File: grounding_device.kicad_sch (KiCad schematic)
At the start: 118 parts, among them IC1 NE555P, IC2 NE555P, IC3 NE555P, IC4 NE555P, Q1 2N2222, Q10 2N2222, Q11 2N2222, Q12 2N2222, Q2 2N2222, Q3 2N2222, Q4 2N2222, Q5 2N2222, Q6 2N2222, Q7 2N2222, Q8 2N2222, Q9 2N2222

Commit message: Upgrade
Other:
- note added: "04.09.2023"
- moved on the sheet: R41
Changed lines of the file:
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@@
   (junction (at 110.49 130.81) (diameter 0) (color 0 0 0 0)
   )
-  (junction (at 261.62 127) (diameter 0) (color 0 0 0 0)
-  )
   (junction (at 99.06 69.85) (diameter 0) (color 0 0 0 0)
   )
@@
   (junction (at 106.68 107.95) (diameter 0) (color 0 0 0 0)
   )
-  (junction (at 264.16 95.25) (diameter 0) (color 0 0 0 0)
-  )
   (junction (at 133.35 15.24) (diameter 0) (color 0 0 0 0)
   )
@@
   (junction (at 217.17 48.26) (diameter 0) (color 0 0 0 0)
   )
+  (junction (at 264.16 48.26) (diameter 0) (color 0 0 0 0)
+  )
   (junction (at 189.23 120.65) (diameter 0) (color 0 0 0 0)
   )
@@
   (junction (at 177.8 95.25) (diameter 0) (color 0 0 0 0)
   )
+  (junction (at 250.19 83.82) (diameter 0) (color 0 0 0 0)
+  )
   (junction (at 115.57 44.45) (diameter 0) (color 0 0 0 0)
   )
@@
     (stroke (width 0) (type default))
   )
+  (wire (pts (xy 279.4 92.71) (xy 250.19 92.71))
+    (stroke (width 0) (type default))
+  )
   (wire (pts (xy 158.75 66.04) (xy 162.56 66.04))
     (stroke (width 0) (type default))
@@
     (stroke (width 0) (type default))
   )
+  (wire (pts (xy 250.19 83.82) (xy 255.27 83.82))
+    (stroke (width 0) (type default))
+  )
   (wire (pts (xy 96.52 83.82) (xy 130.81 83.82))
     (stroke (width 0) (type default))
@@
     (stroke (width 0) (type default))
   )
-  (wire (pts (xy 281.94 113.03) (xy 281.94 127))
-    (stroke (width 0) (type default))
-  )
   (wire (pts (xy 127 166.37) (xy 127 182.88))
     (stroke (width 0) (type default))
@@
     (stroke (width 0) (type default))
   )
-  (wire (pts (xy 281.94 127) (xy 261.62 127))
-    (stroke (width 0) (type default))
-  )
   (wire (pts (xy 139.7 48.26) (xy 154.94 48.26))
     (stroke (width 0) (type default))
@@
     (stroke (width 0) (type default))
   )
+  (wire (pts (xy 250.19 92.71) (xy 250.19 83.82))
+    (stroke (width 0) (type default))
+  )
   (wire (pts (xy 250.19 99.06) (xy 264.16 99.06))
     (stroke (width 0) (type default))
@@
     (stroke (width 0) (type default))
   )
+  (wire (pts (xy 264.16 48.26) (xy 279.4 48.26))
+    (stroke (width 0) (type default))
+  )
   (wire (pts (xy 160.02 104.14) (xy 160.02 93.98))
     (stroke (width 0) (type default))
@@
     (stroke (width 0) (type default))
   )
-  (wire (pts (xy 220.98 83.82) (xy 255.27 83.82))
+  (wire (pts (xy 220.98 83.82) (xy 250.19 83.82))
     (stroke (width 0) (type default))
   )
@@
     (stroke (width 0) (type default))
   )
-  (wire (pts (xy 281.94 95.25) (xy 281.94 102.87))
+  (wire (pts (xy 279.4 48.26) (xy 279.4 82.55))
     (stroke (width 0) (type default))
   )
@@
     (stroke (width 0) (type default))
   )
-  (wire (pts (xy 264.16 95.25) (xy 281.94 95.25))
-    (stroke (width 0) (type default))
-  )
   (wire (pts (xy 256.54 66.04) (xy 256.54 50.8))
     (stroke (width 0) (type default))
@@
     (effects (font (size 1.27 1.27)) (justify left bottom))
   )
+  (text "04.09.2023" (at 270.51 179.07 0)
+    (effects (font (size 1.27 1.27)) (justify left bottom))
+  )
   (text "Klimenko Maxim Sergievich" (at 223.52 185.42 0)
     (effects (font (size 1.27 1.27)) (justify left bottom))
@@
     )
   )
-  (symbol (lib_id "PCM_Elektuur:R") (at 281.94 107.95 0) (mirror y) (unit 1)
+  (symbol (lib_id "PCM_Elektuur:R") (at 279.4 87.63 0) (mirror y) (unit 1)
     (in_bom yes) (on_board yes) (dnp no) (fields_autoplaced)
-    (property "Reference" "R41" (at 279.4 106.68 0)
+    (property "Reference" "R41" (at 276.86 86.36 0)
       (effects (font (size 1.27 1.27)) (justify left))
     )
-    (property "Value" "10-9.5 MOM" (at 279.4 109.22 0)
+    (property "Value" "10-9.5 MOM" (at 276.86 88.9 0)
       (effects (font (size 1.27 1.27)) (justify left))
     )
-    (property "Footprint" "" (at 281.94 107.95 0)
+    (property "Footprint" "" (at 279.4 87.63 0)
       (effects (font (size 1.27 1.27)) hide)
     )
-    (property "Datasheet" "" (at 281.94 107.95 0)
+    (property "Datasheet" "" (at 279.4 87.63 0)
       (effects (font (size 1.27 1.27)) hide)
     )
-    (property "Indicator" "+" (at 285.115 104.775 0)
+    (property "Indicator" "+" (at 282.575 84.455 0)
       (effects (font (size 1.27 1.27)) hide)
     )
-    (property "Rating" "W" (at 279.4 111.125 0)
+    (property "Rating" "W" (at 276.86 90.805 0)
       (effects (font (size 1.27 1.27)) (justify left) hide)
     )

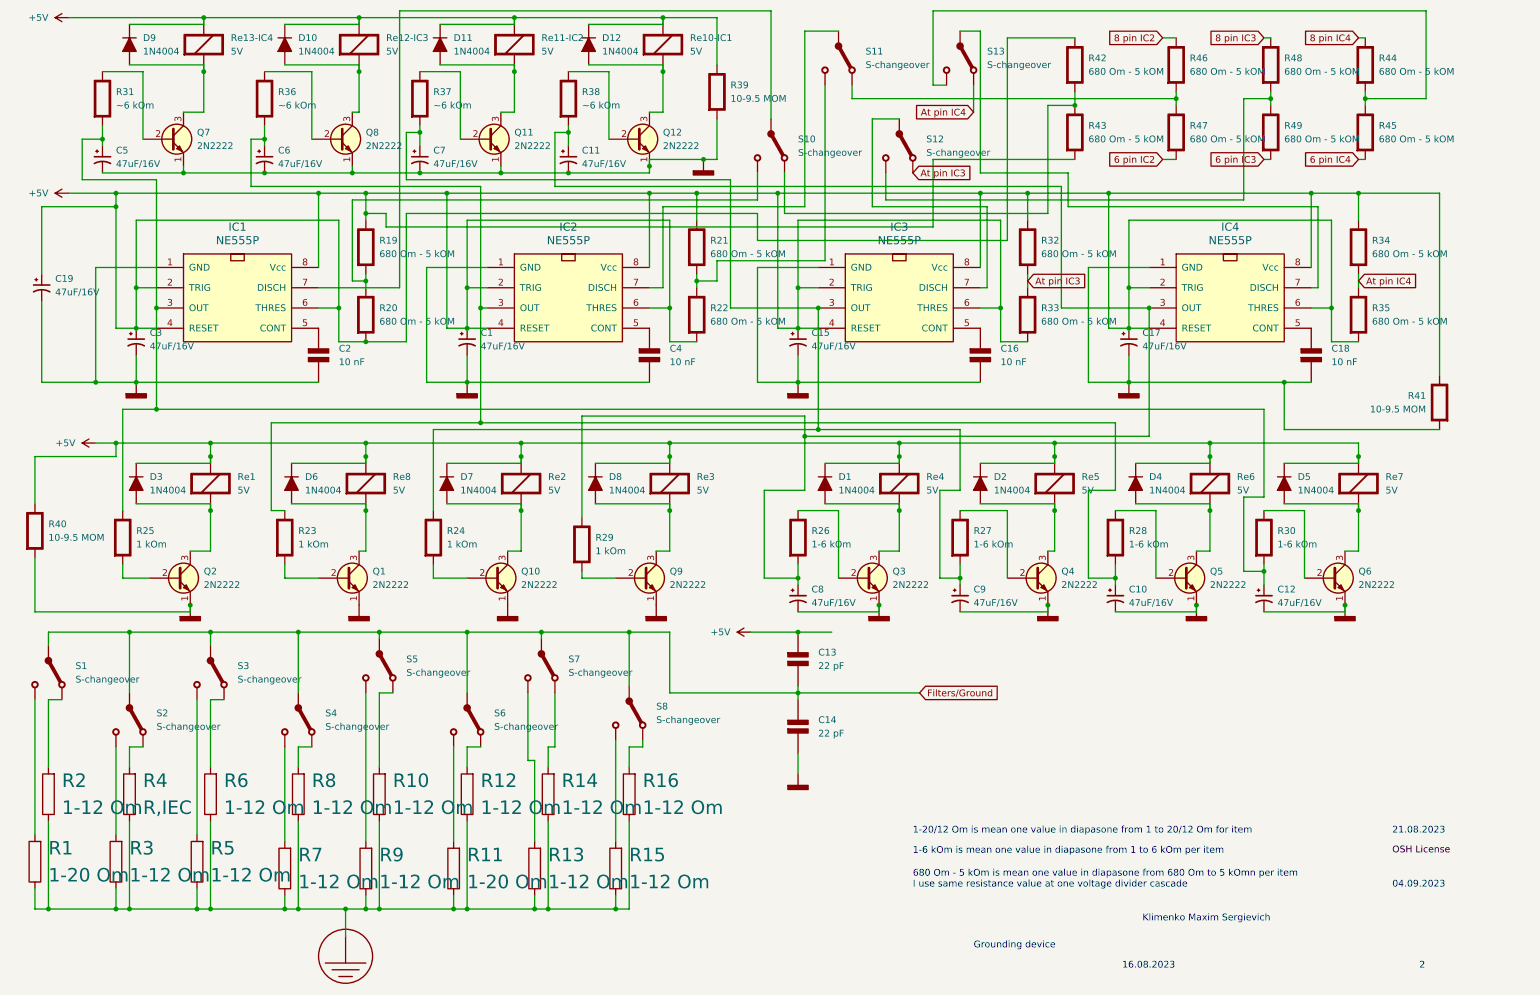
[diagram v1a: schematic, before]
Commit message: Fixed errors in capacitors values
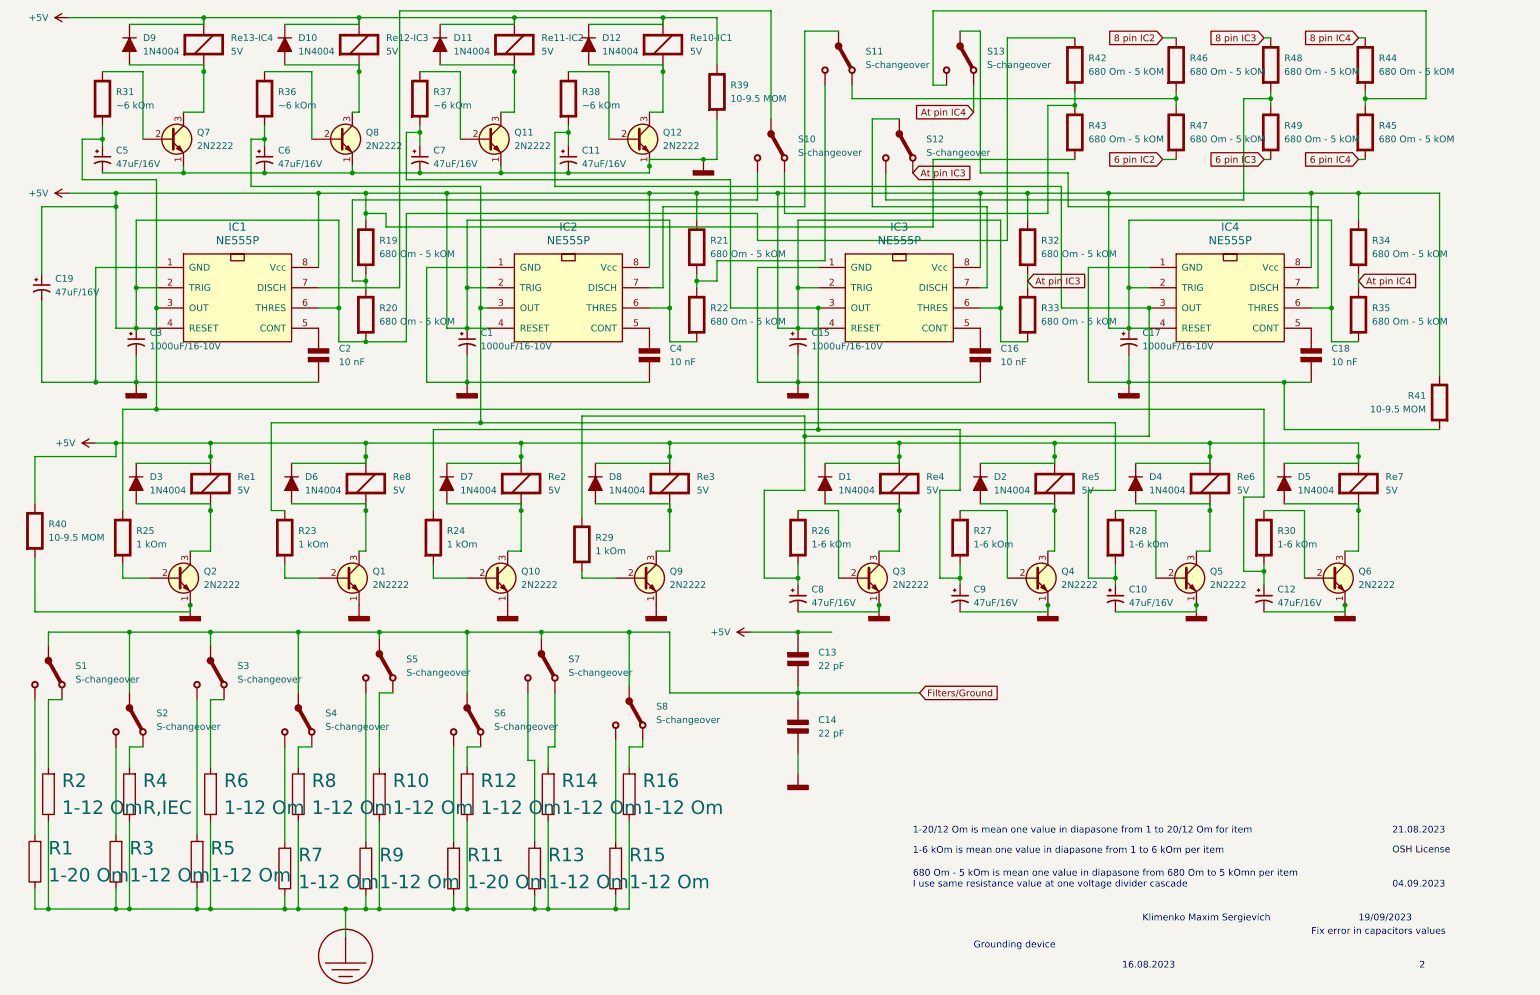
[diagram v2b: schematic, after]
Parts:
- C1, C15, C17, C3: Display 47uF/16V -> 1000uF/16-10V
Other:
- note added: "19/09/2023"
- note added: "Fix error in capacitors values"
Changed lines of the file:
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@@
     (effects (font (size 1.27 1.27)) (justify left bottom))
   )
+  (text "19/09/2023\n" (at 264.16 185.42 0)
+    (effects (font (size 1.27 1.27)) (justify left bottom))
+  )
   (text "Grounding device" (at 191.77 190.5 0)
     (effects (font (size 1.27 1.27)) (justify left bottom))
@@
     (effects (font (size 1.27 1.27)) (justify left bottom))
   )
+  (text "Fix error in capacitors values" (at 255.27 187.96 0)
+    (effects (font (size 1.27 1.27)) (justify left bottom))
+  )
   (label "OSH License" (at 270.51 172.72 0) (fields_autoplaced)
     (effects (font (size 1.27 1.27)) (justify left bottom))
@@
       (effects (font (size 1.27 1.27)) (justify left) hide)
     )
-    (property "Display" "47uF/16V" (at 99.06 77.0382 0)
+    (property "Display" "1000uF/16-10V" (at 99.06 77.0382 0)
       (effects (font (size 1.27 1.27)) (justify left))
     )
@@
       (effects (font (size 1.27 1.27)) (justify left) hide)
     )
-    (property "Display" "47uF/16V" (at 161.29 77.0382 0)
+    (property "Display" "1000uF/16-10V" (at 161.29 77.0382 0)
       (effects (font (size 1.27 1.27)) (justify left))
     )
@@
       (effects (font (size 1.27 1.27)) (justify left) hide)
     )
-    (property "Display" "47uF/16V" (at 36.83 77.0382 0)
+    (property "Display" "1000uF/16-10V" (at 36.83 77.0382 0)
       (effects (font (size 1.27 1.27)) (justify left))
     )
@@
       (effects (font (size 1.27 1.27)) (justify left) hide)
     )
-    (property "Display" "47uF/16V" (at 223.52 77.0382 0)
+    (property "Display" "1000uF/16-10V" (at 223.52 77.0382 0)
       (effects (font (size 1.27 1.27)) (justify left))
     )

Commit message: Fix
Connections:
- net +5V: no longer C1.1, C15.1, C17.1, C3.1, IC1.2 (TRIG), IC1.6 (THRES), IC2.2 (TRIG), IC2.6 (THRES), IC3.2 (TRIG), IC3.6 (THRES), IC4.2 (TRIG), IC4.6 (THRES), R20.2 (-), R22.2 (-), R33.2 (-), R35.2 (-), R42.1 (+)
- new net: C15.1, IC3.2 (TRIG), IC3.6 (THRES), R33.2 (-)
- new net: C1.1, IC2.2 (TRIG), IC2.6 (THRES), R22.2 (-)
- new net: C17.1, IC4.2 (TRIG), IC4.6 (THRES), R35.2 (-)
- new net: C3.1, IC1.2 (TRIG), IC1.6 (THRES), R20.2 (-), R42.1 (+)
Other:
- note added: "680 Om - 5 kOm is mean one value in diapasone from 680 Om to 5 kOmn per item I use same resistance value at one voltage divider cascade ( atennuator )"
- note removed: "680 Om - 5 kOm is mean one value in diapasone from 680 Om to 5 kOmn per item I use same resistance value at one voltage divider cascade"
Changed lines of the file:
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@@
   (junction (at 99.06 69.85) (diameter 0) (color 0 0 0 0)
   )
-  (junction (at 34.29 73.66) (diameter 0) (color 0 0 0 0)
-  )
   (junction (at 106.68 107.95) (diameter 0) (color 0 0 0 0)
   )
@@
   (junction (at 76.2 15.24) (diameter 0) (color 0 0 0 0)
   )
-  (junction (at 158.75 73.66) (diameter 0) (color 0 0 0 0)
-  )
   (junction (at 264.16 97.79) (diameter 0) (color 0 0 0 0)
   )
@@
   (junction (at 45.72 182.88) (diameter 0) (color 0 0 0 0)
   )
-  (junction (at 220.98 73.66) (diameter 0) (color 0 0 0 0)
-  )
   (junction (at 43.18 44.45) (diameter 0) (color 0 0 0 0)
   )
@@
   (junction (at 92.71 48.26) (diameter 0) (color 0 0 0 0)
   )
-  (junction (at 96.52 73.66) (diameter 0) (color 0 0 0 0)
-  )
   (junction (at 46.99 15.24) (diameter 0) (color 0 0 0 0)
   )
@@
     (stroke (width 0) (type default))
   )
-  (wire (pts (xy 34.29 73.66) (xy 30.48 73.66))
+  (wire (pts (xy 30.48 73.66) (xy 38.1 73.66))
     (stroke (width 0) (type default))
   )
@@
     (stroke (width 0) (type default))
   )
-  (wire (pts (xy 220.98 73.66) (xy 217.17 73.66))
+  (wire (pts (xy 217.17 73.66) (xy 224.79 73.66))
     (stroke (width 0) (type default))
   )
@@
     (stroke (width 0) (type default))
   )
-  (wire (pts (xy 158.75 73.66) (xy 154.94 73.66))
-    (stroke (width 0) (type default))
-  )
-  (wire (pts (xy 162.56 73.66) (xy 158.75 73.66))
+  (wire (pts (xy 154.94 73.66) (xy 162.56 73.66))
     (stroke (width 0) (type default))
   )
@@
     (stroke (width 0) (type default))
   )
-  (wire (pts (xy 38.1 73.66) (xy 34.29 73.66))
-    (stroke (width 0) (type default))
-  )
   (wire (pts (xy 152.4 104.14) (xy 160.02 104.14))
     (stroke (width 0) (type default))
@@
     (stroke (width 0) (type default))
   )
-  (wire (pts (xy 224.79 73.66) (xy 220.98 73.66))
-    (stroke (width 0) (type default))
-  )
   (wire (pts (xy 30.48 50.8) (xy 30.48 48.26))
     (stroke (width 0) (type default))
@@
     (stroke (width 0) (type default))
   )
-  (wire (pts (xy 96.52 73.66) (xy 92.71 73.66))
+  (wire (pts (xy 92.71 73.66) (xy 100.33 73.66))
     (stroke (width 0) (type default))
   )
@@
   )
   (wire (pts (xy 34.29 53.34) (xy 72.39 53.34))
-    (stroke (width 0) (type default))
-  )
-  (wire (pts (xy 100.33 73.66) (xy 96.52 73.66))
     (stroke (width 0) (type default))
   )
@@
     (effects (font (size 1.27 1.27)) (justify left bottom))
   )
-  (text "680 Om - 5 kOm is mean one value in diapasone from 680 Om to 5 kOmn per item \nI use same resistance value at one voltage divider cascade"
+  (text "680 Om - 5 kOm is mean one value in diapasone from 680 Om to 5 kOmn per item \nI use same resistance value at one voltage divider cascade ( atennuator )"
     (at 180.34 179.07 0)
     (effects (font (size 1.27 1.27)) (justify left bottom))
